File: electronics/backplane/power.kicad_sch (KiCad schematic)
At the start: 0 parts

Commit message: Continue backplane
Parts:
- added C1, C2, C3: 10u_X7R_2012M, Applidyne_Capacitor:CAPC2012X110N, symbol appli_capacitor:10u_X7R_2012M
- added R12: 10K0_1608M, Applidyne_Resistor:RESC1608X50N, symbol appli_resistor:10K0_1608M
- added U9: AP2112K-3.3, Applidyne_SOT:SOT95P280X145-5L30N, symbol appli_regulator:AP2112K-3.3
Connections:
- new net: C1.1, R12.1, U9.1 (VIN)
- new net: R12.2, U9.3 (EN)
- new net +3.3V: C2.1, C3.1, U9.5 (VOUT)
- new net GND: C1.2, C2.2, C3.2, U9.2 (GND)

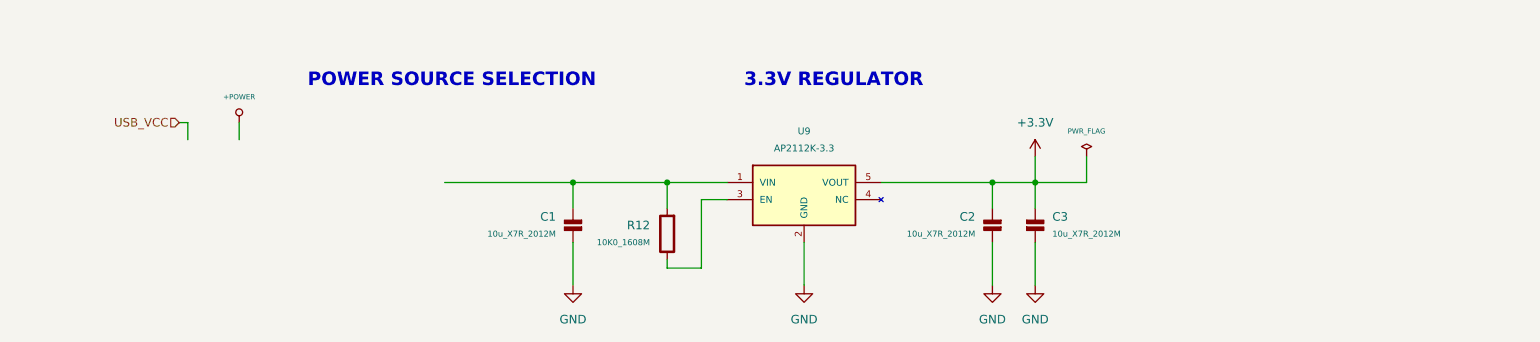
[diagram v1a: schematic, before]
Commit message: Continue schematic tweaks, start routing backplane
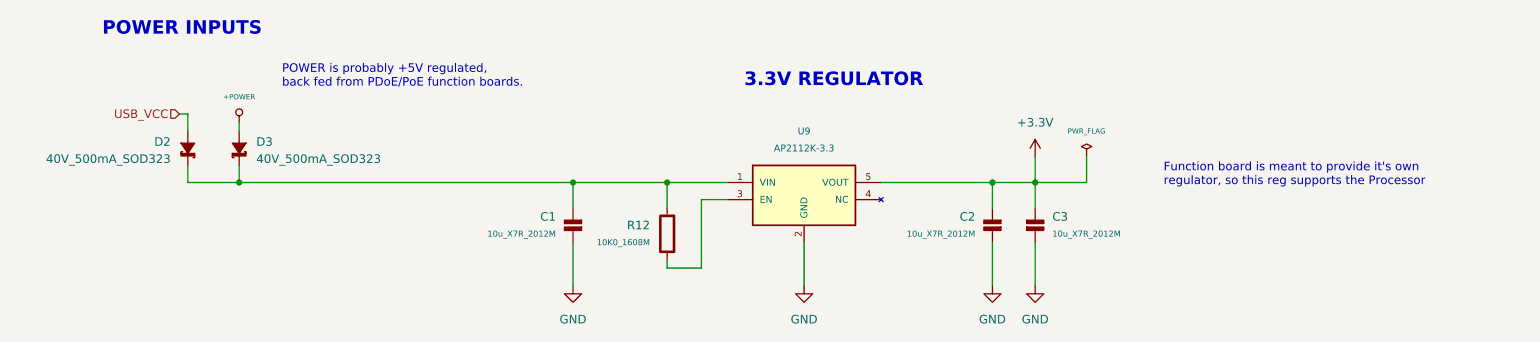
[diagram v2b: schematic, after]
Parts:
- added D2, D3: 40V_500mA_SOD323, Applidyne_SOD:SOD2512X110N, symbol appli_device:40V_500mA_SOD323
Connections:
- net +POWER: now also D3.A
- net USB_VCC: now also D2.A
- net at C1.1, R12.1, U9.1 (VIN): now also D2.C, D3.C
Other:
- note added: "Function board is meant to provide it's own regulator, so this reg supports the Processor"
- note added: "POWER INPUTS"
- note added: "POWER is probably +5V regulated, back fed from PDoE/PoE function boards."
- note removed: "POWER SOURCE SELECTION"
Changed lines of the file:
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@@
   (junction (at 149.86 55.88) (diameter 0) (color 0 0 0 0)
   )
+  (junction (at 86.36 55.88) (diameter 0) (color 0 0 0 0)
+  )
   (wire (pts (xy 198.12 64.77) (xy 198.12 71.12))
     (stroke (width 0) (type default))
@@
     (stroke (width 0) (type default))
   )
+  (wire (pts (xy 86.36 53.34) (xy 86.36 55.88))
+    (stroke (width 0) (type default))
+  )
   (wire (pts (xy 170.18 64.77) (xy 170.18 71.12))
     (stroke (width 0) (type default))
   )
-  (wire (pts (xy 86.36 46.99) (xy 86.36 49.53))
+  (wire (pts (xy 86.36 46.99) (xy 86.36 48.26))
     (stroke (width 0) (type default))
   )
@@
     (stroke (width 0) (type default))
   )
+  (wire (pts (xy 78.74 53.34) (xy 78.74 55.88))
+    (stroke (width 0) (type default))
+  )
   (wire (pts (xy 198.12 55.88) (xy 198.12 59.69))
     (stroke (width 0) (type default))
@@
     (stroke (width 0) (type default))
   )
-  (wire (pts (xy 116.84 55.88) (xy 135.89 55.88))
-    (stroke (width 0) (type default))
-  )
-  (wire (pts (xy 77.47 46.99) (xy 78.74 46.99))
+  (wire (pts (xy 78.74 55.88) (xy 86.36 55.88))
+    (stroke (width 0) (type default))
+  )
+  (wire (pts (xy 77.47 45.72) (xy 78.74 45.72))
     (stroke (width 0) (type default))
   )
@@
     (stroke (width 0) (type default))
   )
+  (wire (pts (xy 86.36 55.88) (xy 135.89 55.88))
+    (stroke (width 0) (type default))
+  )
   (wire (pts (xy 149.86 55.88) (xy 149.86 59.69))
     (stroke (width 0) (type default))
@@
     (stroke (width 0) (type default))
   )
-  (wire (pts (xy 78.74 46.99) (xy 78.74 49.53))
+  (wire (pts (xy 78.74 45.72) (xy 78.74 48.26))
     (stroke (width 0) (type default))
   )
@@
     (effects (font (size 2 2) (thickness 0.4) bold) (justify left bottom))
   )
-  (text "POWER SOURCE SELECTION" (at 96.52 41.91 0)
+  (text "POWER INPUTS" (at 66.04 34.29 0)
     (effects (font (size 2 2) (thickness 0.4) bold) (justify left bottom))
   )
-  (hierarchical_label "USB_VCC" (shape input) (at 77.47 46.99 180) (fields_autoplaced)
+  (text "POWER is probably +5V regulated,\nback fed from PDoE/PoE function boards."
+    (at 92.71 41.91 0)
+    (effects (font (size 1.27 1.27)) (justify left bottom))
+  )
+  (text "Function board is meant to provide it's own\nregulator, so this reg supports the Processor"
+    (at 223.52 56.515 0)
+    (effects (font (size 1.27 1.27)) (justify left bottom))
+  )
+  (hierarchical_label "USB_VCC" (shape input) (at 77.47 45.72 180) (fields_autoplaced)
     (effects (font (size 1.27 1.27)) (justify right))
   )
@@
     )
   )
+  (symbol (lib_id "appli_device:40V_500mA_SOD323") (at 86.36 50.8 90) (unit 1)
+    (in_bom yes) (on_board yes) (dnp no) (fields_autoplaced)
+    (property "Reference" "D3" (at 88.9 49.8475 90)
+      (effects (font (size 1.27 1.27)) (justify right))
+    )
+    (property "Value" "40V_500mA_SOD323" (at 88.9 52.3875 90)
+      (effects (font (size 1.27 1.27)) (justify right))
+    )
+    (property "Footprint" "Applidyne_SOD:SOD2512X110N" (at 90.17 50.8 0)
+      (effects (font (size 0.508 0.508)) hide)
+    )
+    (property "Datasheet" "http://www.farnell.com/datasheets/684565.pdf" (at 90.805 50.8 0)
+      (effects (font (size 0.508 0.508)) hide)
+    )
+    (property "manf" "NXP" (at 92.075 50.8 0)
+      (effects (font (size 0.508 0.508)) hide)
+    )
+    (property "manf#" "PMEG4005AEA" (at 92.71 50.8 0)
+      (effects (font (size 0.508 0.508)) hide)
+    )
+    (property "Supplier" "Element14" (at 93.345 50.8 0)
+      (effects (font (size 0.508 0.508)) hide)
+    )
+    (property "Supplier Part No" "8738025" (at 93.98 50.8 0)
+      (effects (font (size 0.508 0.508)) hide)
+    )
+    (property "Supplier URL" "http://au.element14.com/nxp/pmeg4005aea/diode-schottky-sod-323/dp/8738025" (at 94.615 50.8 0)
+      (effects (font (size 0.508 0.508)) hide)
+    )
+    (property "Supplier Price" "0.044" (at 95.25 50.8 0)
+      (effects (font (size 0.508 0.508)) hide)
+    )
+    (property "Supplier Price Break" "1" (at 95.885 50.8 0)
+      (effects (font (size 0.508 0.508)) hide)
+    )
+    (pin "A")
+    (pin "C")
+    (instances
+      (project "backplane"
+        (path "/0bfdf1e4-b99d-46d4-adfc-42d352d37946/8f621588-890f-4fc0-9198-4ddb5e4e0920"
+          (reference "D3") (unit 1)
+        )
+      )
+    )
+  )
   (symbol (lib_id "appli_power:GND") (at 198.12 71.12 0) (unit 1)
     (in_bom yes) (on_board yes) (dnp no) (fields_autoplaced)
@@
         )
       )
+    )
+  )
+  (symbol (lib_id "appli_device:40V_500mA_SOD323") (at 78.74 50.8 270) (mirror x) (unit 1)
+    (in_bom yes) (on_board yes) (dnp no)
+    (property "Reference" "D2" (at 76.2 49.8475 90)
+      (effects (font (size 1.27 1.27)) (justify right))
+    )
+    (property "Value" "40V_500mA_SOD323" (at 76.2 52.3875 90)
+      (effects (font (size 1.27 1.27)) (justify right))
+    )
+    (property "Footprint" "Applidyne_SOD:SOD2512X110N" (at 74.93 50.8 0)
+      (effects (font (size 0.508 0.508)) hide)
+    )
+    (property "Datasheet" "http://www.farnell.com/datasheets/684565.pdf" (at 74.295 50.8 0)
+      (effects (font (size 0.508 0.508)) hide)
+    )
+    (property "manf" "NXP" (at 73.025 50.8 0)
+      (effects (font (size 0.508 0.508)) hide)
+    )
+    (property "manf#" "PMEG4005AEA" (at 72.39 50.8 0)
+      (effects (font (size 0.508 0.508)) hide)
+    )
+    (property "Supplier" "Element14" (at 71.755 50.8 0)
+      (effects (font (size 0.508 0.508)) hide)
+    )
+    (property "Supplier Part No" "8738025" (at 71.12 50.8 0)
+      (effects (font (size 0.508 0.508)) hide)
+    )
+    (property "Supplier URL" "http://au.element14.com/nxp/pmeg4005aea/diode-schottky-sod-323/dp/8738025" (at 70.485 50.8 0)
+      (effects (font (size 0.508 0.508)) hide)
+    )
+    (property "Supplier Price" "0.044" (at 69.85 50.8 0)
+      (effects (font (size 0.508 0.508)) hide)
+    )
+    (property "Supplier Price Break" "1" (at 69.215 50.8 0)
+      (effects (font (size 0.508 0.508)) hide)
+    )
+    (pin "A")
+    (pin "C")
+    (instances
+      (project "backplane"
+        (path "/0bfdf1e4-b99d-46d4-adfc-42d352d37946/8f621588-890f-4fc0-9198-4ddb5e4e0920"
+          (reference "D2") (unit 1)
+        )
+      )

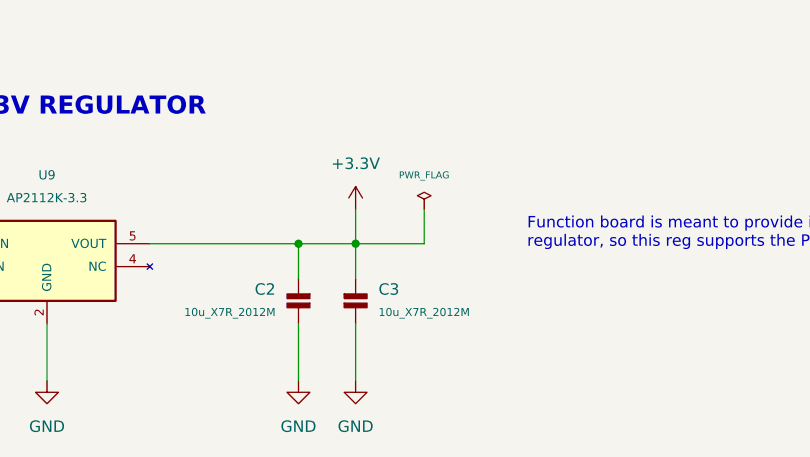
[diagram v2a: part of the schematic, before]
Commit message: Continue backplane design Cleanup schematic, most routing and placement done
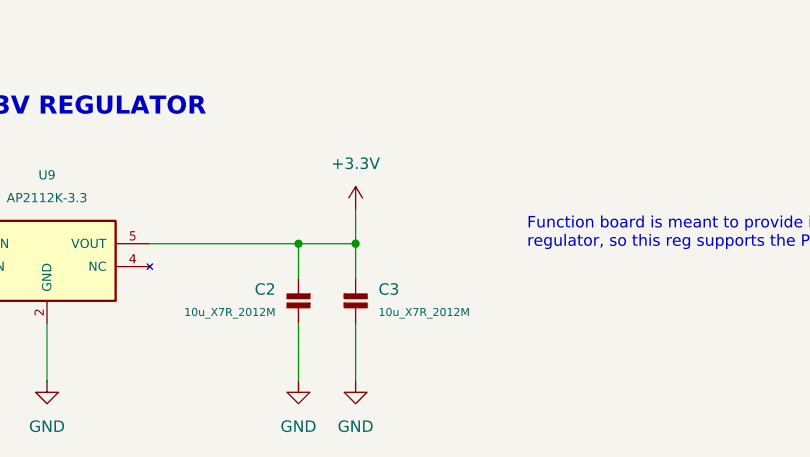
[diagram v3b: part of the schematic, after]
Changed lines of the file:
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@@
-    (stroke (width 0) (type default))
-  )
-  (wire (pts (xy 212.09 52.07) (xy 212.09 55.88))
     (stroke (width 0) (type default))
   )
@@
   )
   (wire (pts (xy 149.86 55.88) (xy 149.86 59.69))
-    (stroke (width 0) (type default))
-  )
-  (wire (pts (xy 204.47 55.88) (xy 212.09 55.88))
     (stroke (width 0) (type default))
   )
@@
         )
       )
-    )
-  )
-  (symbol (lib_id "appli_power:PWR_FLAG") (at 212.09 52.07 0) (unit 1)
-    (in_bom yes) (on_board yes) (dnp no)
-    (property "Reference" "#FLG01" (at 212.09 50.8 0)
-      (effects (font (size 0.762 0.762)) hide)
-    )
-    (property "Value" "PWR_FLAG" (at 212.09 48.26 0)
-      (effects (font (size 0.762 0.762)))
-    )
-    (property "Footprint" "" (at 212.09 52.07 0)
-      (effects (font (size 1.524 1.524)))
-    )
-    (property "Datasheet" "" (at 212.09 52.07 0)
-      (effects (font (size 1.524 1.524)))
-    )
-    (pin "1")
-    (instances
-      (project "backplane"
-        (path "/0bfdf1e4-b99d-46d4-adfc-42d352d37946/8f621588-890f-4fc0-9198-4ddb5e4e0920"
-          (reference "#FLG01") (unit 1)
-        )
-      )

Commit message: Backplane routing complete General schematic cleanup, board cosmetics etc
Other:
- title: (none) -> REGULATION
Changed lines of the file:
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@@
 (kicad_sch (version 20230121) (generator eeschema)
   (paper "A4")
+  (title_block
+    (title "REGULATION")
+    (date "2023-08-09")
+    (rev "V1.0")
+  )
   (junction (at 204.47 55.88) (diameter 0) (color 0 0 0 0)
   )
